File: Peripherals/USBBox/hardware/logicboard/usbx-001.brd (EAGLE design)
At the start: 91 x 57 mm, 10 parts, among them J2 AUDIO_JACK_TRRSSMD_RA, J7 DIN5, J8 DIN5

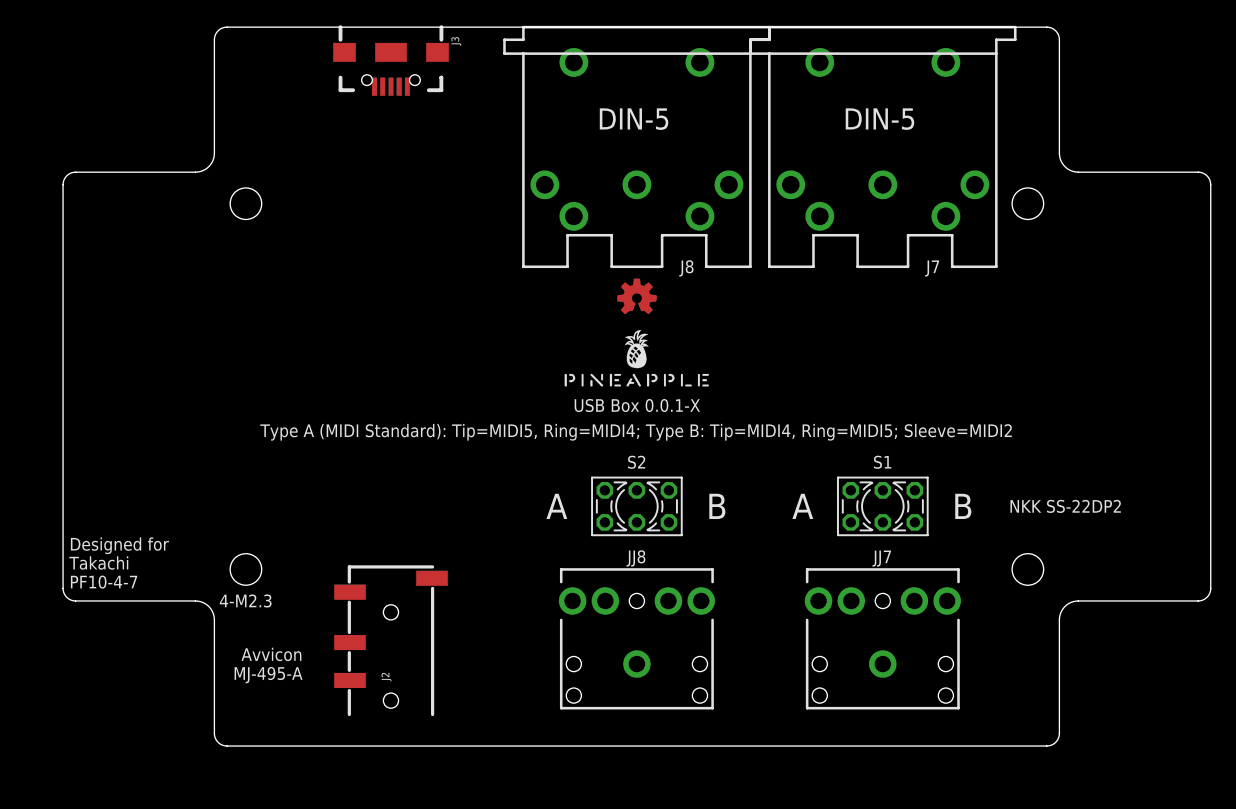
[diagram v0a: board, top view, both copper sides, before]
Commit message: New form factor.
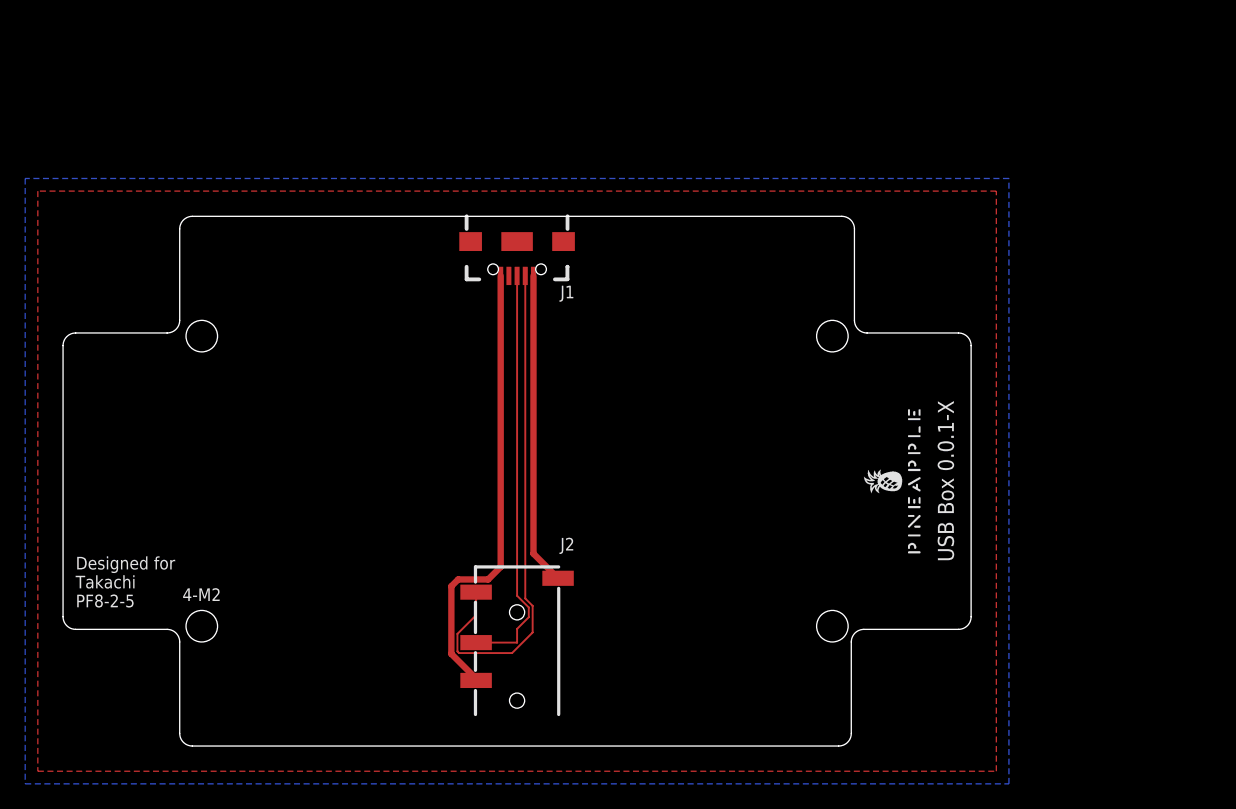
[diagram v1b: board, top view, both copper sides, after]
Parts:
- removed J3: (no value), SparkFun-Connectors:USB-B-MICRO-SMD_RED_PASTE
- removed J7, J8: DIN5, SparkFun-Connectors:DIN5-RA-PTH
- removed JJ7, JJ8: AUDIO_JACK_3.5MM_KIT, SparkFun-Connectors:AUDIO-JACK-KIT
- removed LOGO1: OSHW-LOGOS-COPPER, SparkFun-Aesthetics:OSHW-LOGO-S_COPPER
- removed S1, S2: 9450-2, switch-misc:9450-2
- added J1: (no value), SparkFun-Connectors:USB-B-MICRO-SMD
- U$1: value PINEAPPLE450 -> PINEAPPLE450_SILK; device pineapple:PINEAPPLE450 -> pineapple:PINEAPPLE450_SILK
- moved U$1 23.7 mm to (68.0, 21.0), turned to 90 degrees
- moved J2 10.0 mm to (36.0, 2.00)
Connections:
- removed net M1GND: J7.2, JJ7.SLEEVE
- removed net M1RING: JJ7.TIP, S1.3, S1.4
- removed net M1RTN: J7.5, S1.2
- removed net M1SND: J7.4, S1.5
- removed net M1TIP: JJ7.RING, S1.1, S1.6
- removed net M2GND: J8.2, JJ8.SLEEVE
- removed net M2RING: JJ8.TIP, S2.3, S2.4
- removed net M2RTN: J8.5, S2.2
- removed net M2SND: J8.4, S2.5
- removed net M2TIP: JJ8.RING, S2.1, S2.6
- net D+: now also J1.D+; no longer J3.D+
- net D-: now also J1.D-; no longer J3.D-
- net GND: now also J1.GND; no longer J3.GND
- net VBUS: now also J1.VBUS; no longer J3.VBUS
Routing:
- net D-: track 0.00 -> 40.5 mm
- net GND: track 0.00 -> 35.9 mm
- net D+: track 0.00 -> 33.1 mm
- net VBUS: track 0.00 -> 24.8 mm
- added copper zone on layer 1, net GND
- added copper zone on layer 16, net GND
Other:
- board size 91 x 57 mm -> 72 x 42 mm
- board text added: "4-M2"
- board text added: "Designed for Takachi PF8-2-5"
- board text removed: "4-M2.3"
- board text removed: "A"
- board text removed: "Avvicon MJ-495-A"
- board text removed: "B"
- board text removed: "Designed for Takachi PF10-4-7"
- board text removed: "GND"
- board text removed: "NKK SS-22DP2"
- board text removed: "RNG"
- board text removed: "RTN"
- board text removed: "SLV"
- board text removed: "SND"
- board text removed: "TIP"
- board text removed: "Type A (MIDI Standard): Tip=MIDI5, Ring=MIDI4; Type B: Tip=MIDI4, Ring=MIDI5; Sleeve=MIDI2"

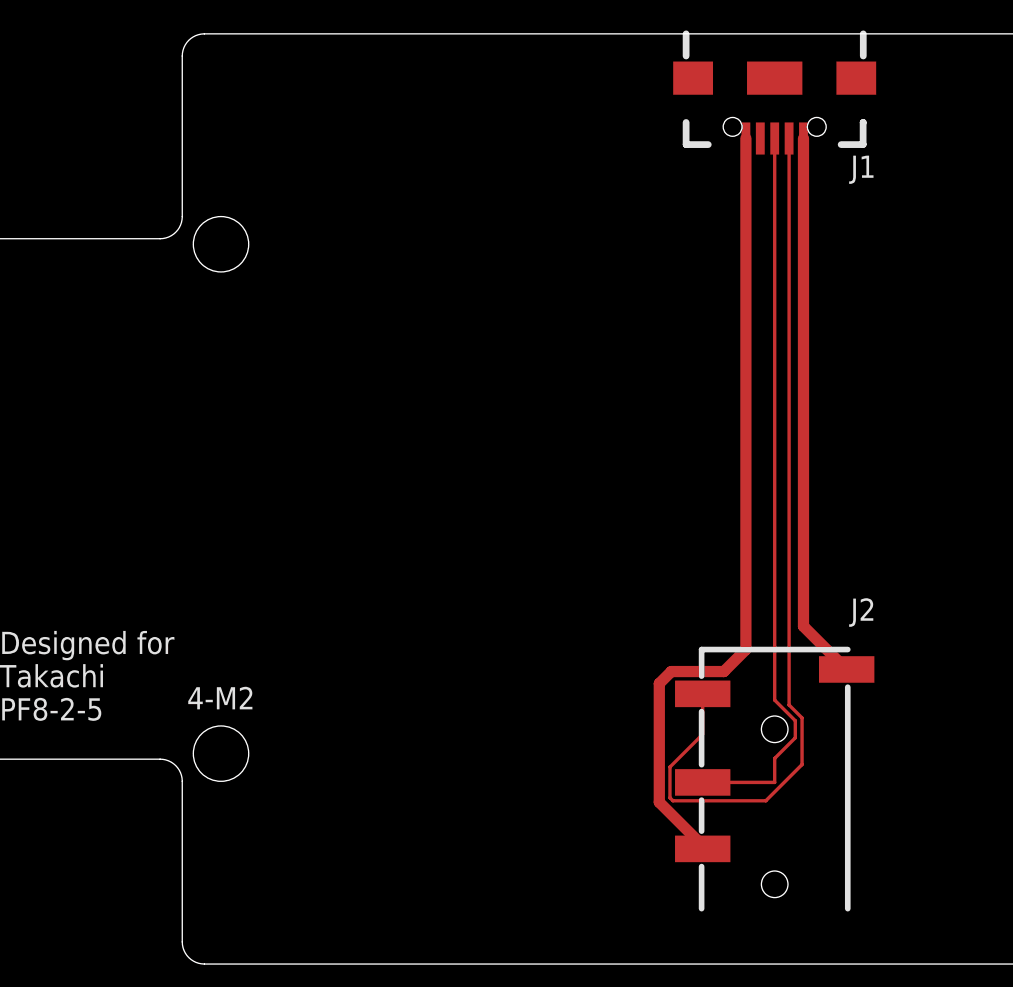
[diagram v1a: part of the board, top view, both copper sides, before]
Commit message: Added resistors for iPod shuffle compatibility.
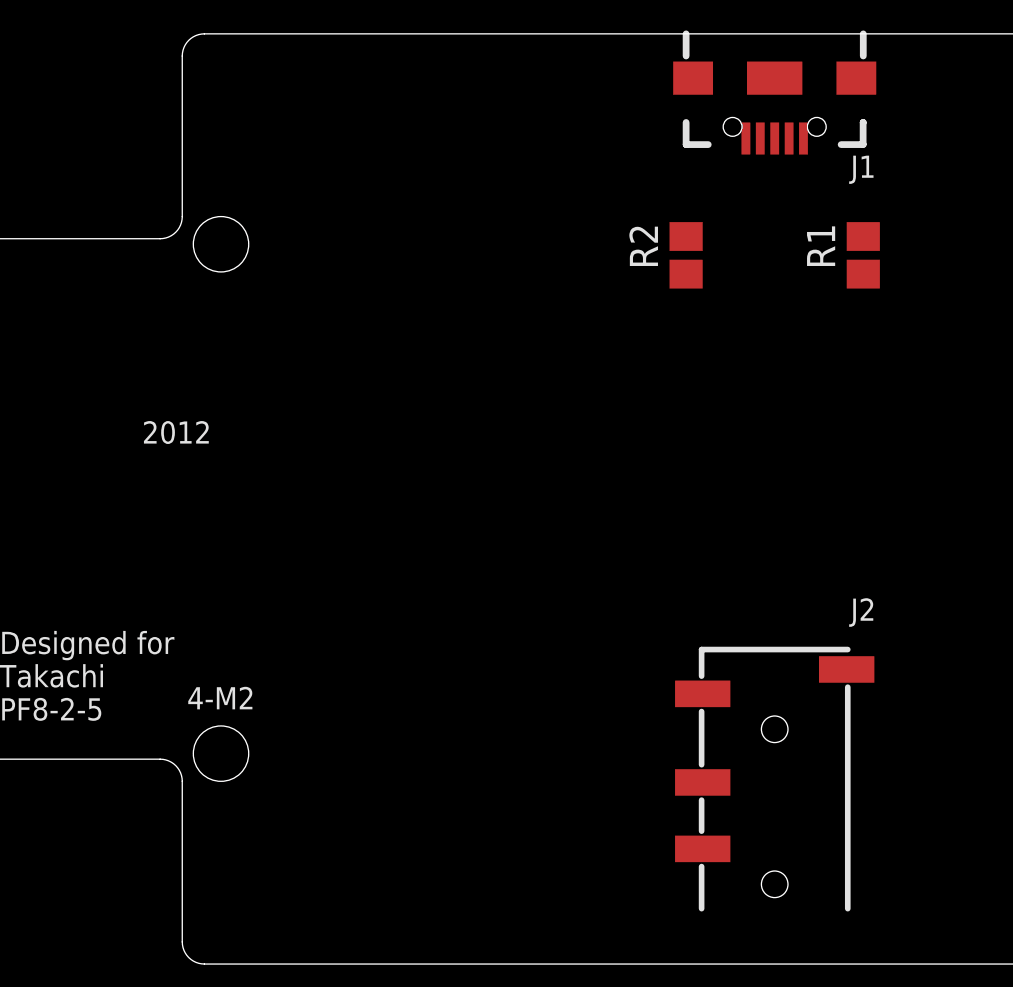
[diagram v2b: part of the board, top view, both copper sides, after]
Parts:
- added R1: 120, rcl:R2012
- added R2: 200, rcl:R2012
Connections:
- new net VBUSR: J2.EARTH, R1.1, R2.1
- net GND: now also R2.2
- net VBUS: now also R1.2; no longer J2.EARTH
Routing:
- net D-: track 40.5 -> 0.00 mm
- net GND: track 35.9 -> 0.00 mm
- net D+: track 33.1 -> 0.00 mm
- net VBUS: track 24.8 -> 0.00 mm
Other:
- board text added: "2012"
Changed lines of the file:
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@@
 <setting verticaltext="up"/>
 </settings>
-<grid distance="1" unitdist="mm" unit="mm" style="lines" multiple="2" display="yes" altdistance="50" altunitdist="mil" altunit="mil"/>
+<grid distance="0.05" unitdist="mm" unit="mm" style="lines" multiple="2" display="yes" altdistance="50" altunitdist="mil" altunit="mil"/>
 <layers>
 <layer number="1" name="Top" color="4" fill="1" visible="yes" active="yes"/>
@@
 PF8-2-5</text>
 <text x="11" y="12" size="1" layer="25" align="center">4-M2</text>
+<text x="9" y="24" size="1" layer="25" align="center">2012</text>
 </plain>
 <attributes>
@@
 <attribute name="VALUE" x="37.397" y="5.175" size="0.6096" layer="27" font="vector" ratio="20" rot="R90"/>
 </element>
+<element name="R1" library="rcl" library_urn="urn:adsk.eagle:library:334" package="R2012" package3d_urn="urn:adsk.eagle:package:23543/2" value="120" x="40" y="32" smashed="yes" rot="R90">
+<attribute name="NAME" x="38.73" y="31.365" size="1.27" layer="25" rot="R90"/>
+<attribute name="POPULARITY" value="0" x="40" y="32" size="1.778" layer="27" rot="R90" display="off"/>
+<attribute name="SPICEPREFIX" value="R" x="40" y="32" size="1.778" layer="27" rot="R90" display="off"/>
+<attribute name="VALUE" x="42.54" y="31.365" size="1.27" layer="27" rot="R90"/>
+</element>
+<element name="R2" library="rcl" library_urn="urn:adsk.eagle:library:334" package="R2012" package3d_urn="urn:adsk.eagle:package:23543/2" value="200" x="32" y="32" smashed="yes" rot="R90">
+<attribute name="NAME" x="30.73" y="31.365" size="1.27" layer="25" rot="R90"/>
+<attribute name="POPULARITY" value="0" x="32" y="32" size="1.778" layer="27" rot="R90" display="off"/>
+<attribute name="SPICEPREFIX" value="R" x="32" y="32" size="1.778" layer="27" rot="R90" display="off"/>
+<attribute name="VALUE" x="34.54" y="31.365" size="1.27" layer="27" rot="R90"/>
+</element>
 </elements>
 <signals>
@@
 <contactref element="J1" pad="GND"/>
 <contactref element="J2" pad="RING2"/>
-<wire x1="34.7" y1="37.275" x2="34.7" y2="14.2" width="0.508" layer="1"/>
-<wire x1="32.75" y1="5.3442125" x2="32.75" y2="5.2" width="0.508" layer="1"/>
-<wire x1="30.7888" y1="7.3054125" x2="32.75" y2="5.3442125" width="0.508" layer="1"/>
-<wire x1="31.3316625" y1="13.2064" x2="30.7888" y2="12.6635375" width="0.508" layer="1"/>
-<wire x1="30.7888" y1="12.6635375" x2="30.7888" y2="7.3054125" width="0.508" layer="1"/>
-<wire x1="34.7" y1="14.2" x2="33.7064" y2="13.2064" width="0.508" layer="1"/>
-<wire x1="33.7064" y1="13.2064" x2="31.3316625" y2="13.2064" width="0.508" layer="1"/>
 <polygon width="0.2" layer="1">
 <vertex x="-2" y="-2"/>
@@
 <vertex x="-3" y="45"/>
 </polygon>
-</signal>
-<signal name="VBUS" class="2">
-<contactref element="J1" pad="VBUS"/>
-<contactref element="J2" pad="EARTH"/>
-<wire x1="37.3" y1="37.275" x2="37.3" y2="15.25" width="0.508" layer="1"/>
-<wire x1="37.3" y1="15.25" x2="39.25" y2="13.3" width="0.508" layer="1"/>
+<contactref element="R2" pad="2"/>
+<wire x1="32" y1="32.85" x2="34.7" y2="37.275" width="0" layer="19" extent="1-1"/>
+<wire x1="32.75" y1="5.2" x2="32" y2="32.85" width="0" layer="19" extent="1-1"/>
 </signal>
 <signal name="D-">
 <contactref element="J1" pad="D-"/>
 <contactref element="J2" pad="TIP"/>
-<wire x1="31.4053125" y1="7.3714" x2="31.2714" y2="7.5053125" width="0.1524" layer="1"/>
-<wire x1="31.2714" y1="7.5053125" x2="31.2714" y2="8.8946875" width="0.1524" layer="1"/>
-<wire x1="36.65" y1="11.6965625" x2="37.235" y2="11.1115625" width="0.1524" layer="1"/>
-<wire x1="36.65" y1="37.275" x2="36.65" y2="11.6965625" width="0.1524" layer="1"/>
-<wire x1="37.235" y1="11.1115625" x2="37.235" y2="9.00394375" width="0.1524" layer="1"/>
-<wire x1="37.235" y1="9.00394375" x2="35.60245625" y2="7.3714" width="0.1524" layer="1"/>
-<wire x1="35.60245625" y1="7.3714" x2="31.4053125" y2="7.3714" width="0.1524" layer="1"/>
-<wire x1="31.2714" y1="8.8946875" x2="32.75" y2="10.3732875" width="0.1524" layer="1"/>
-<wire x1="32.75" y1="10.3732875" x2="32.75" y2="12.2" width="0.1524" layer="1"/>
+<wire x1="32.75" y1="12.2" x2="36.65" y2="37.275" width="0" layer="19" extent="1-1"/>
 </signal>
 <signal name="D+">
 <contactref element="J1" pad="D+"/>
 <contactref element="J2" pad="RING1"/>
-<wire x1="36.9302" y1="10.98530625" x2="36.9302" y2="10.21469375" width="0.1524" layer="1"/>
-<wire x1="36" y1="37.275" x2="36" y2="11.91550625" width="0.1524" layer="1"/>
-<wire x1="36" y1="9.28449375" x2="36" y2="8.2" width="0.1524" layer="1"/>
-<wire x1="36" y1="11.91550625" x2="36.9302" y2="10.98530625" width="0.1524" layer="1"/>
-<wire x1="36.9302" y1="10.21469375" x2="36" y2="9.28449375" width="0.1524" layer="1"/>
-<wire x1="36" y1="8.2" x2="32.75" y2="8.2" width="0.1524" layer="1"/>
+<wire x1="32.75" y1="8.2" x2="36" y2="37.275" width="0" layer="19" extent="1-1"/>
+</signal>
+<signal name="VBUS" class="2">
+<contactref element="J1" pad="VBUS"/>
+<contactref element="R1" pad="2"/>
+<wire x1="40" y1="32.85" x2="37.3" y2="37.275" width="0" layer="19" extent="1-1"/>
+</signal>
+<signal name="VBUSR" class="2">
+<contactref element="R1" pad="1"/>
+<contactref element="J2" pad="EARTH"/>
+<contactref element="R2" pad="1"/>
+<wire x1="32" y1="31.15" x2="40" y2="31.15" width="0" layer="19" extent="1-1"/>
+<wire x1="39.25" y1="13.3" x2="40" y2="31.15" width="0" layer="19" extent="1-1"/>
 </signal>
 </signals>
